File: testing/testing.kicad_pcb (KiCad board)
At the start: 2 copper layers, 106.8 x 66.8 mm, 0 parts

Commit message: Test Commit 11
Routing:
- net (no net): vias 38 -> 19
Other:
- board size 106.8 x 66.8 mm -> 45.8 x 63.6 mm
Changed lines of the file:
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@@
-	)
-	(gr_line
-		(start 85.11 96.52)
-		(end 74.315 115.57)
-		(stroke
-			(width 0.2)
-			(type default)
-		)
-		(layer "F.Cu")
 	)
 	(gr_line
 		(start 146.05 93.345)
 		(end 135.255 112.395)
-		(stroke
-			(width 0.2)
-			(type default)
-		)
-		(layer "F.Cu")
-	)
-	(gr_line
-		(start 74.315 115.57)
-		(end 95.27 120.015)
 		(stroke
 			(width 0.2)
@@
 		(layer "Edge.Cuts")
 	)
-	(gr_rect
-		(start 60.96 69.725)
-		(end 106.81 133.325)
-		(stroke
-			(width 0.05)
-			(type default)
-		)
-		(fill no)
-		(layer "Edge.Cuts")
-	)
 	(via
 		(at 133.35 85.09)
-		(size 0.6)
-		(drill 0.3)
-		(layers "F.Cu" "B.Cu")
-		(net 0)
-	)
-	(via
-		(at 69.87 89.535)
 		(size 0.6)
 		(drill 0.3)
@@
 	)
 	(via
-		(at 71.14 100.33)
-		(size 0.6)
-		(drill 0.3)
-		(layers "F.Cu" "B.Cu")
-		(net 0)
-	)
-	(via
-		(at 66.06 102.87)
-		(size 0.6)
-		(drill 0.3)
-		(layers "F.Cu" "B.Cu")
-		(net 0)
-	)
-	(via
 		(at 125.095 105.41)
 		(size 0.6)
@@
 	)
 	(via
-		(at 72.41 88.265)
-		(size 0.6)
-		(drill 0.3)
-		(layers "F.Cu" "B.Cu")
-		(net 0)
-	)
-	(via
 		(at 138.43 82.55)
-		(size 0.6)
-		(drill 0.3)
-		(layers "F.Cu" "B.Cu")
-		(net 0)
-	)
-	(via
-		(at 85.745 92.075)
-		(size 0.6)
-		(drill 0.3)
-		(layers "F.Cu" "B.Cu")
-		(net 0)
-	)
-	(via
-		(at 87.65 86.36)
 		(size 0.6)
 		(drill 0.3)
@@
 	)
 	(via
-		(at 70.505 93.98)
-		(size 0.6)
-		(drill 0.3)
-		(layers "F.Cu" "B.Cu")
-		(net 0)
-	)
-	(via
 		(at 148.59 83.185)
 		(size 0.6)
@@
 	)
 	(via
-		(at 92.73 83.82)
-		(size 0.6)
-		(drill 0.3)
-		(layers "F.Cu" "B.Cu")
-		(net 0)
-	)
-	(via
-		(at 87.015 81.915)
-		(size 0.6)
-		(drill 0.3)
-		(layers "F.Cu" "B.Cu")
-		(net 0)
-	)
-	(via
 		(at 137.795 85.725)
 		(size 0.6)
@@
 	)
 	(via
-		(at 92.095 86.995)
-		(size 0.6)
-		(drill 0.3)
-		(layers "F.Cu" "B.Cu")
-		(net 0)
-	)
-	(via
-		(at 76.855 88.9)
-		(size 0.6)
-		(drill 0.3)
-		(layers "F.Cu" "B.Cu")
-		(net 0)
-	)
-	(via
-		(at 64.155 108.585)
-		(size 0.6)
-		(drill 0.3)
-		(layers "F.Cu" "B.Cu")
-		(net 0)
-	)
-	(via
-		(at 71.14 107.95)
-		(size 0.6)
-		(drill 0.3)
-		(layers "F.Cu" "B.Cu")
-		(net 0)
-	)
-	(via
-		(at 77.49 85.725)
-		(size 0.6)
-		(drill 0.3)
-		(layers "F.Cu" "B.Cu")
-		(net 0)
-	)
-	(via
-		(at 85.11 87.63)
-		(size 0.6)
-		(drill 0.3)
-		(layers "F.Cu" "B.Cu")
-		(net 0)
-	)
-	(via
 		(at 127 99.695)
-		(size 0.6)
-		(drill 0.3)
-		(layers "F.Cu" "B.Cu")
-		(net 0)
-	)
-	(via
-		(at 77.49 93.345)
-		(size 0.6)
-		(drill 0.3)
-		(layers "F.Cu" "B.Cu")
-		(net 0)
-	)
-	(via
-		(at 70.505 103.505)
-		(size 0.6)
-		(drill 0.3)
-		(layers "F.Cu" "B.Cu")
-		(net 0)
-	)
-	(via
-		(at 63.52 104.14)
-		(size 0.6)
-		(drill 0.3)
-		(layers "F.Cu" "B.Cu")
-		(net 0)
-	)
-	(via
-		(at 92.73 91.44)
 		(size 0.6)
 		(drill 0.3)
@@
 			)
 		)
-	)
-	(zone
-		(net 0)
-		(net_name "")
-		(layer "B.Cu")
-		(hatch edge 0.5)
-		(connect_pads
-			(clearance 0.5)
-		)
-		(min_thickness 0.25)
-		(filled_areas_thickness no)
-		(fill yes
-			(thermal_gap 0.5)
-			(thermal_bridge_width 0.5)
-			(island_removal_mode 1)
-			(island_area_min 10)
-		)
-		(polygon
-			(pts
-				(xy 60.96 69.725) (xy 60.96 133.325) (xy 106.81 133.325) (xy 106.81 69.725)
-			)
-		)

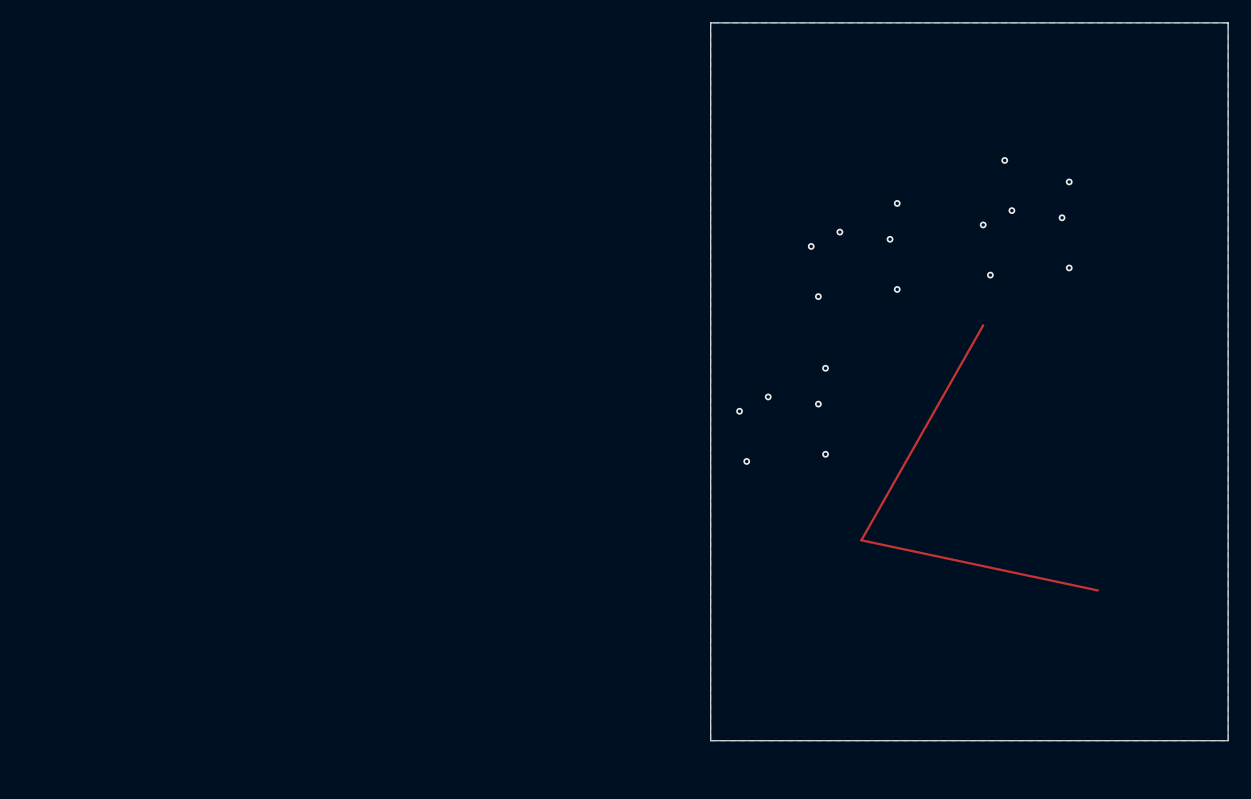
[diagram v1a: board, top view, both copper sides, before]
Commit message: Test Commit 10 + Removed test.yml
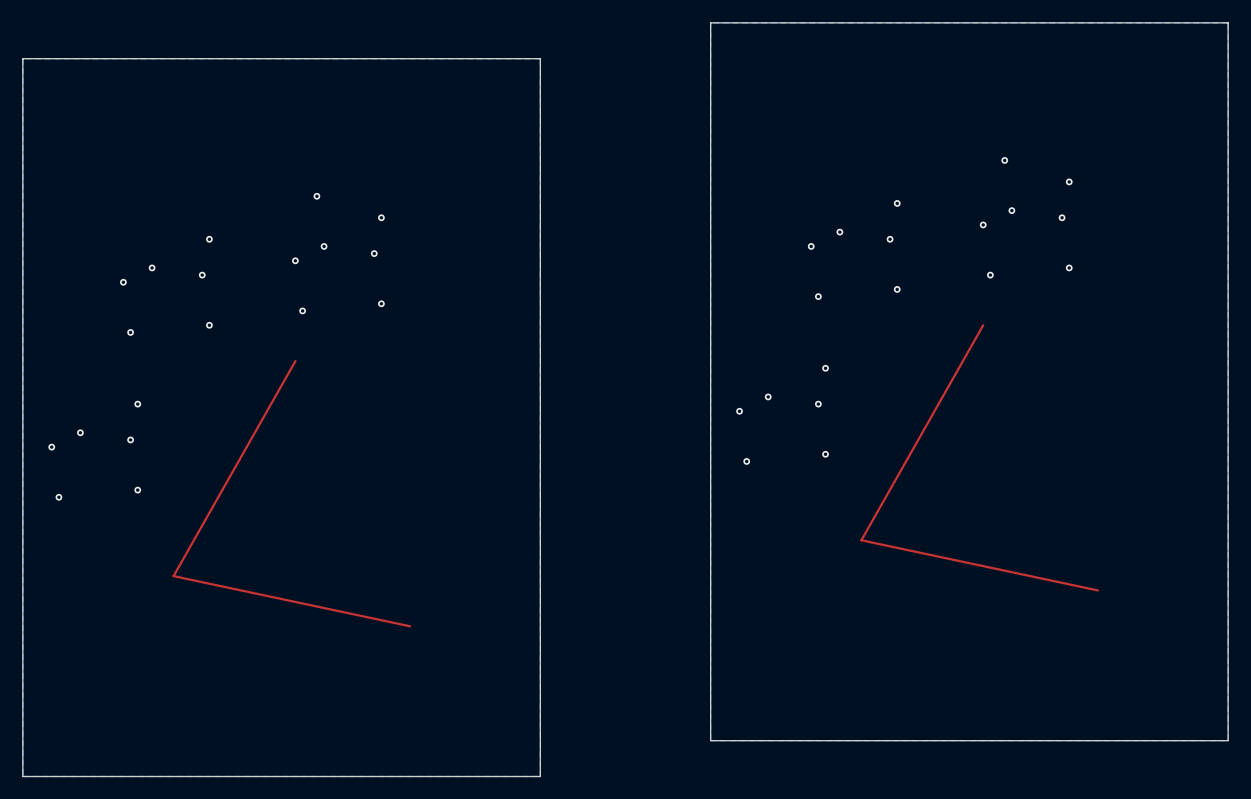
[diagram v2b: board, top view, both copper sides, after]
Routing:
- net (no net): vias 19 -> 38
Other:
- board size 45.8 x 63.6 mm -> 106.8 x 66.8 mm
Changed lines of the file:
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@@
+	)
+	(gr_line
+		(start 85.11 96.52)
+		(end 74.315 115.57)
+		(stroke
+			(width 0.2)
+			(type default)
+		)
+		(layer "F.Cu")
 	)
 	(gr_line
@@
 		(layer "F.Cu")
 	)
+	(gr_line
+		(start 74.315 115.57)
+		(end 95.27 120.015)
+		(stroke
+			(width 0.2)
+			(type default)
+		)
+		(layer "F.Cu")
+	)
 	(gr_rect
 		(start 121.9 66.55)
@@
 		(layer "Edge.Cuts")
 	)
+	(gr_rect
+		(start 60.96 69.725)
+		(end 106.81 133.325)
+		(stroke
+			(width 0.05)
+			(type default)
+		)
+		(fill no)
+		(layer "Edge.Cuts")
+	)
 	(via
 		(at 133.35 85.09)
@@
 	)
 	(via
+		(at 69.87 89.535)
+		(size 0.6)
+		(drill 0.3)
+		(layers "F.Cu" "B.Cu")
+		(net 0)
+	)
+	(via
 		(at 146.685 88.9)
 		(size 0.6)
@@
 	)
 	(via
+		(at 71.14 100.33)
+		(size 0.6)
+		(drill 0.3)
+		(layers "F.Cu" "B.Cu")
+		(net 0)
+	)
+	(via
+		(at 66.06 102.87)
+		(size 0.6)
+		(drill 0.3)
+		(layers "F.Cu" "B.Cu")
+		(net 0)
+	)
+	(via
 		(at 125.095 105.41)
 		(size 0.6)
@@
 	)
 	(via
+		(at 72.41 88.265)
+		(size 0.6)
+		(drill 0.3)
+		(layers "F.Cu" "B.Cu")
+		(net 0)
+	)
+	(via
 		(at 138.43 82.55)
 		(size 0.6)
@@
 	)
 	(via
+		(at 85.745 92.075)
+		(size 0.6)
+		(drill 0.3)
+		(layers "F.Cu" "B.Cu")
+		(net 0)
+	)
+	(via
+		(at 87.65 86.36)
+		(size 0.6)
+		(drill 0.3)
+		(layers "F.Cu" "B.Cu")
+		(net 0)
+	)
+	(via
 		(at 153.67 88.265)
 		(size 0.6)
@@
 	)
 	(via
+		(at 70.505 93.98)
+		(size 0.6)
+		(drill 0.3)
+		(layers "F.Cu" "B.Cu")
+		(net 0)
+	)
+	(via
 		(at 148.59 83.185)
 		(size 0.6)
@@
 	)
 	(via
+		(at 92.73 83.82)
+		(size 0.6)
+		(drill 0.3)
+		(layers "F.Cu" "B.Cu")
+		(net 0)
+	)
+	(via
+		(at 87.015 81.915)
+		(size 0.6)
+		(drill 0.3)
+		(layers "F.Cu" "B.Cu")
+		(net 0)
+	)
+	(via
 		(at 137.795 85.725)
 		(size 0.6)
@@
 	)
 	(via
+		(at 92.095 86.995)
+		(size 0.6)
+		(drill 0.3)
+		(layers "F.Cu" "B.Cu")
+		(net 0)
+	)
+	(via
+		(at 76.855 88.9)
+		(size 0.6)
+		(drill 0.3)
+		(layers "F.Cu" "B.Cu")
+		(net 0)
+	)
+	(via
+		(at 64.155 108.585)
+		(size 0.6)
+		(drill 0.3)
+		(layers "F.Cu" "B.Cu")
+		(net 0)
+	)
+	(via
+		(at 71.14 107.95)
+		(size 0.6)
+		(drill 0.3)
+		(layers "F.Cu" "B.Cu")
+		(net 0)
+	)
+	(via
+		(at 77.49 85.725)
+		(size 0.6)
+		(drill 0.3)
+		(layers "F.Cu" "B.Cu")
+		(net 0)
+	)
+	(via
+		(at 85.11 87.63)
+		(size 0.6)
+		(drill 0.3)
+		(layers "F.Cu" "B.Cu")
+		(net 0)
+	)
+	(via
 		(at 127 99.695)
+		(size 0.6)
+		(drill 0.3)
+		(layers "F.Cu" "B.Cu")
+		(net 0)
+	)
+	(via
+		(at 77.49 93.345)
+		(size 0.6)
+		(drill 0.3)
+		(layers "F.Cu" "B.Cu")
+		(net 0)
+	)
+	(via
+		(at 70.505 103.505)
+		(size 0.6)
+		(drill 0.3)
+		(layers "F.Cu" "B.Cu")
+		(net 0)
+	)
+	(via
+		(at 63.52 104.14)
+		(size 0.6)
+		(drill 0.3)
+		(layers "F.Cu" "B.Cu")
+		(net 0)
+	)
+	(via
+		(at 92.73 91.44)
 		(size 0.6)
 		(drill 0.3)
@@
 			)
 		)
+	)
+	(zone
+		(net 0)
+		(net_name "")
+		(layer "B.Cu")
+		(hatch edge 0.5)
+		(connect_pads
+			(clearance 0.5)
+		)
+		(min_thickness 0.25)
+		(filled_areas_thickness no)
+		(fill yes
+			(thermal_gap 0.5)
+			(thermal_bridge_width 0.5)
+			(island_removal_mode 1)
+			(island_area_min 10)
+		)
+		(polygon
+			(pts
+				(xy 60.96 69.725) (xy 60.96 133.325) (xy 106.81 133.325) (xy 106.81 69.725)
+			)
+		)
